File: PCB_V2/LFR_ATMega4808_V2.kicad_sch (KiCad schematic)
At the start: 74 parts, among them J1 Conn_02x02_Odd_Even, J10 Conn_01x03, J11 Conn_01x03, J2 Conn_02x05_Odd_Even, J5 Conn_01x03, J6 Conn_02x03_Odd_Even, J7 Conn_02x02_Odd_Even, J8 Conn_01x03, J9 Conn_01x03, Q1 PMOS_Si2333DDS, Q10 NMOS_BSR802NL6327HTSA1, Q11 NMOS_BSR802NL6327HTSA1, Q5 NMOS_BSR802NL6327HTSA1, Q6 NMOS_BSR802NL6327HTSA1, Q7 NMOS_BSR802NL6327HTSA1, Q8 NMOS_BSR802NL6327HTSA1, Q9 PMOS_Si2333DDS, U1 ATmega4808-A, U5 MCP1700x-330xxTO

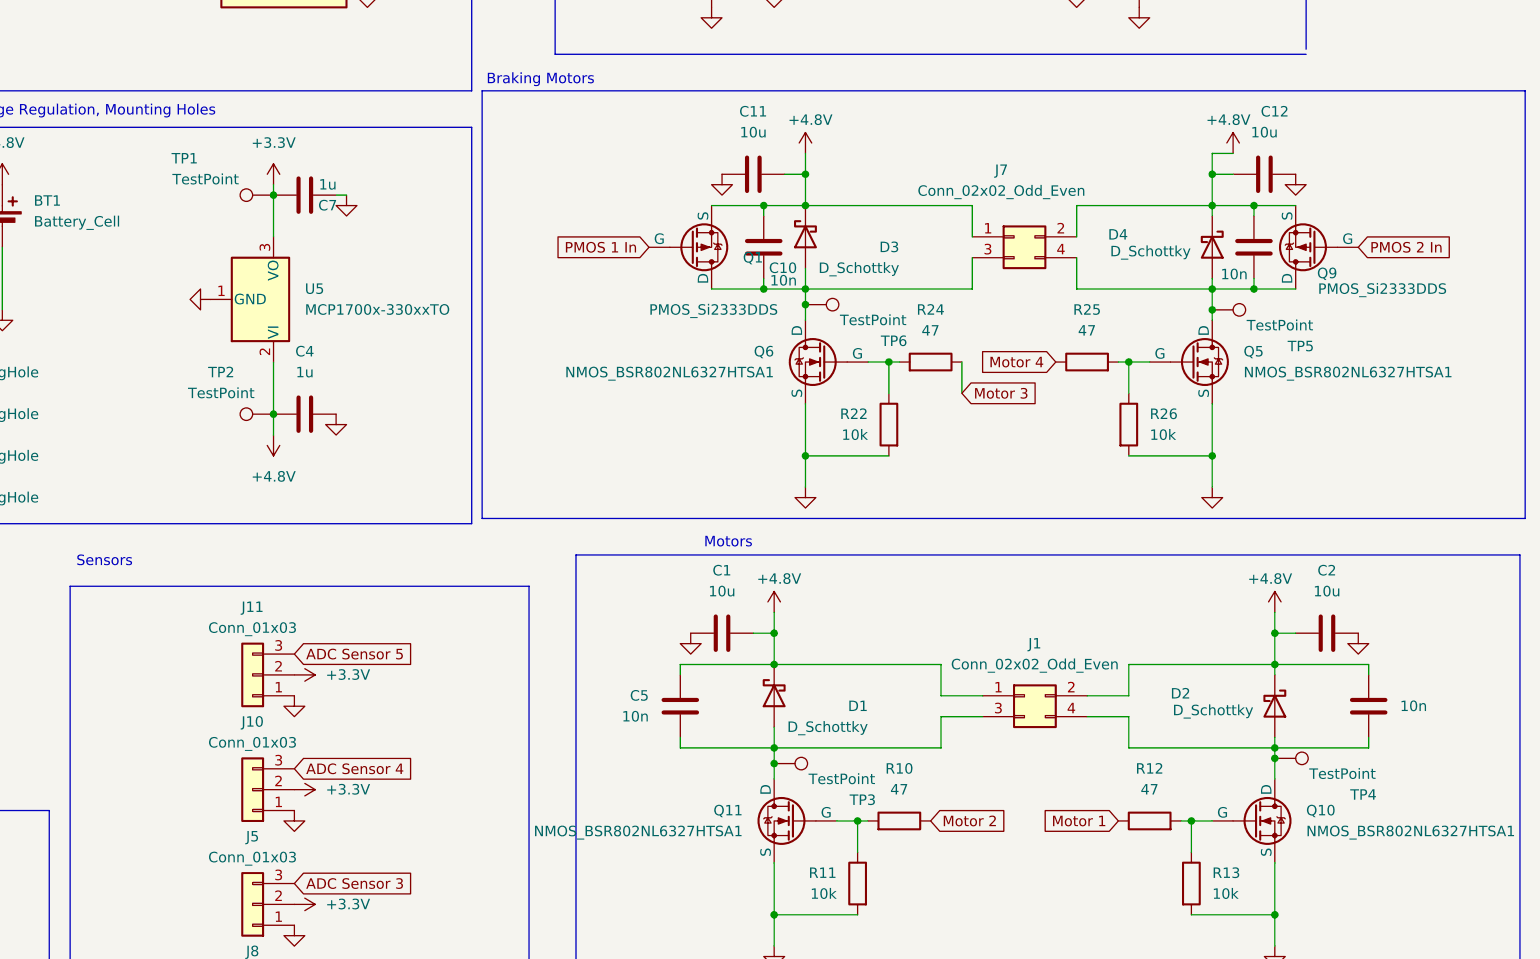
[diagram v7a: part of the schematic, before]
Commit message: Changed labels
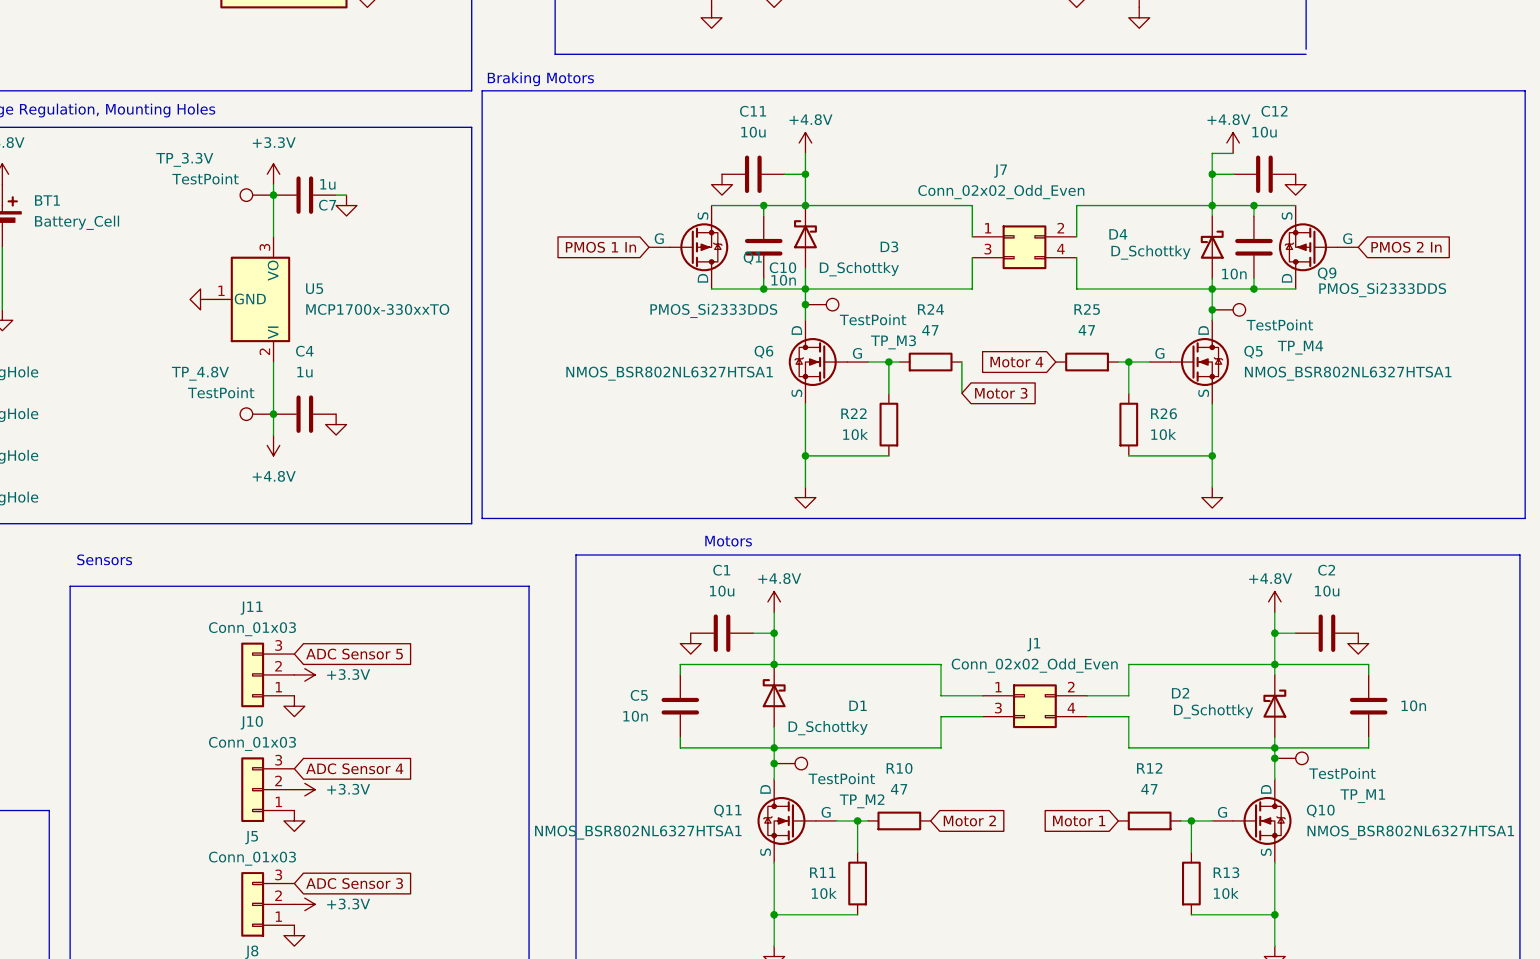
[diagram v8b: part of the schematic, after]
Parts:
- renumbered TP1 to TP_3.3V, TP2 to TP_4.8V, TP4 to TP_M1, TP3 to TP_M2, TP6 to TP_M3, TP5 to TP_M4
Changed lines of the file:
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@@
 		(in_pos_files yes)
 		(dnp no)
-		(property "Reference" "TP4"
+		(property "Reference" "TP_M1"
 			(at 264.795 139.065 90)
 			(show_name no)
@@
 			(project "LFR_ATMega4808_V2"
 				(path "/7fcd8b9a-e9e6-4d51-9258-8399f733a0d2"
-					(reference "TP4")
+					(reference "TP_M1")
 					(unit 1)
 				)
@@
 		(in_pos_files yes)
 		(dnp no)
-		(property "Reference" "TP2"
-			(at 125.73 87.63 90)
+		(property "Reference" "TP_4.8V"
+			(at 123.19 87.63 90)
 			(show_name no)
 			(do_not_autoplace no)
@@
 			(project "LFR_ATMega4808_V2"
 				(path "/7fcd8b9a-e9e6-4d51-9258-8399f733a0d2"
-					(reference "TP2")
+					(reference "TP_4.8V")
 					(unit 1)
 				)
@@
 		(in_pos_files yes)
 		(dnp no)
-		(property "Reference" "TP3"
+		(property "Reference" "TP_M2"
 			(at 203.835 139.7 90)
 			(show_name no)
@@
 			(project "LFR_ATMega4808_V2"
 				(path "/7fcd8b9a-e9e6-4d51-9258-8399f733a0d2"
-					(reference "TP3")
+					(reference "TP_M2")
 					(unit 1)
 				)
@@
 		(in_pos_files yes)
 		(dnp no)
-		(property "Reference" "TP5"
+		(property "Reference" "TP_M4"
 			(at 257.175 84.455 90)
 			(show_name no)
@@
 			(project "LFR_ATMega4808_V2"
 				(path "/7fcd8b9a-e9e6-4d51-9258-8399f733a0d2"
-					(reference "TP5")
+					(reference "TP_M4")
 					(unit 1)
 				)
@@
 		(in_pos_files yes)
 		(dnp no)
-		(property "Reference" "TP6"
+		(property "Reference" "TP_M3"
 			(at 207.645 83.82 90)
 			(show_name no)
@@
 			(project "LFR_ATMega4808_V2"
 				(path "/7fcd8b9a-e9e6-4d51-9258-8399f733a0d2"
-					(reference "TP6")
+					(reference "TP_M3")
 					(unit 1)
 				)
@@
 		(in_pos_files yes)
 		(dnp no)
-		(property "Reference" "TP1"
+		(property "Reference" "TP_3.3V"
 			(at 121.285 61.595 90)
 			(show_name no)
@@
 			(project "LFR_ATMega4808_V2"
 				(path "/7fcd8b9a-e9e6-4d51-9258-8399f733a0d2"
-					(reference "TP1")
+					(reference "TP_3.3V")
 					(unit 1)
 				)
